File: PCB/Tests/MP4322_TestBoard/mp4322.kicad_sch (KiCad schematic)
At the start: 28 parts, among them J1 Conn_01x02, J2 Conn_01x02, U7 MP4322GDE-P

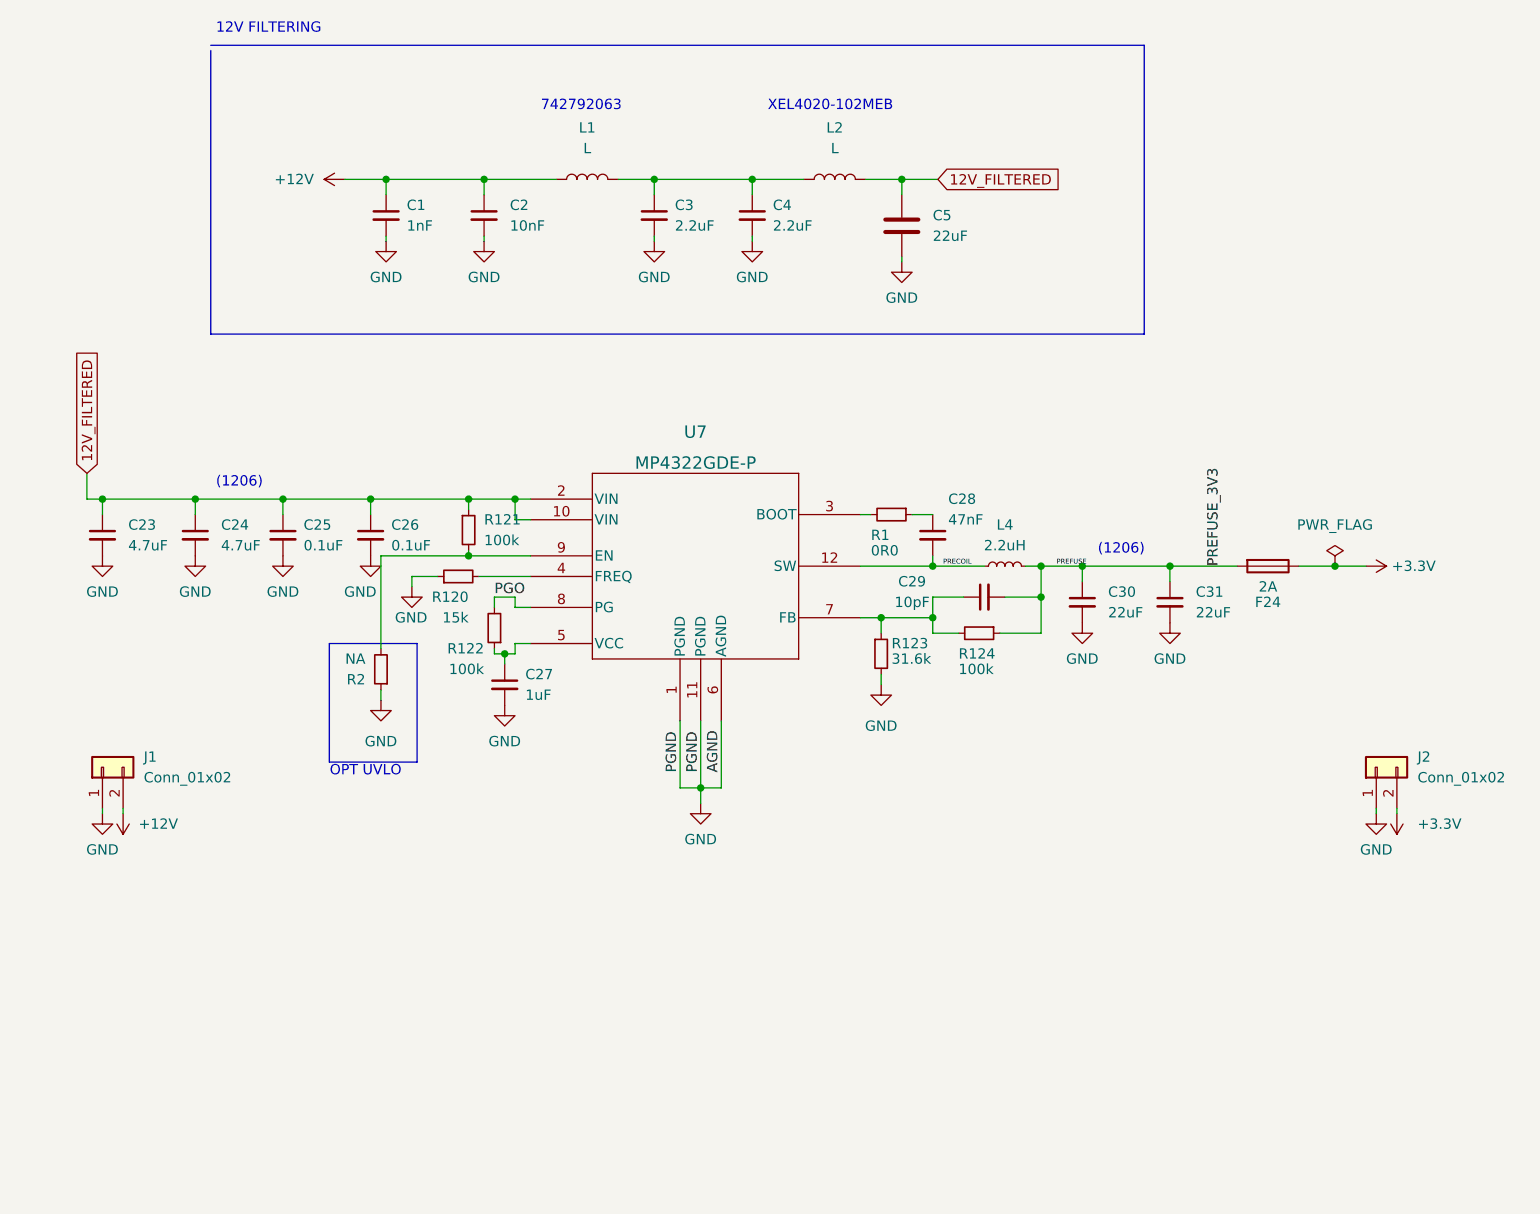
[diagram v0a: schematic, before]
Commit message: Generated production files for RP_MPQ5850 & MP4322 schematic change
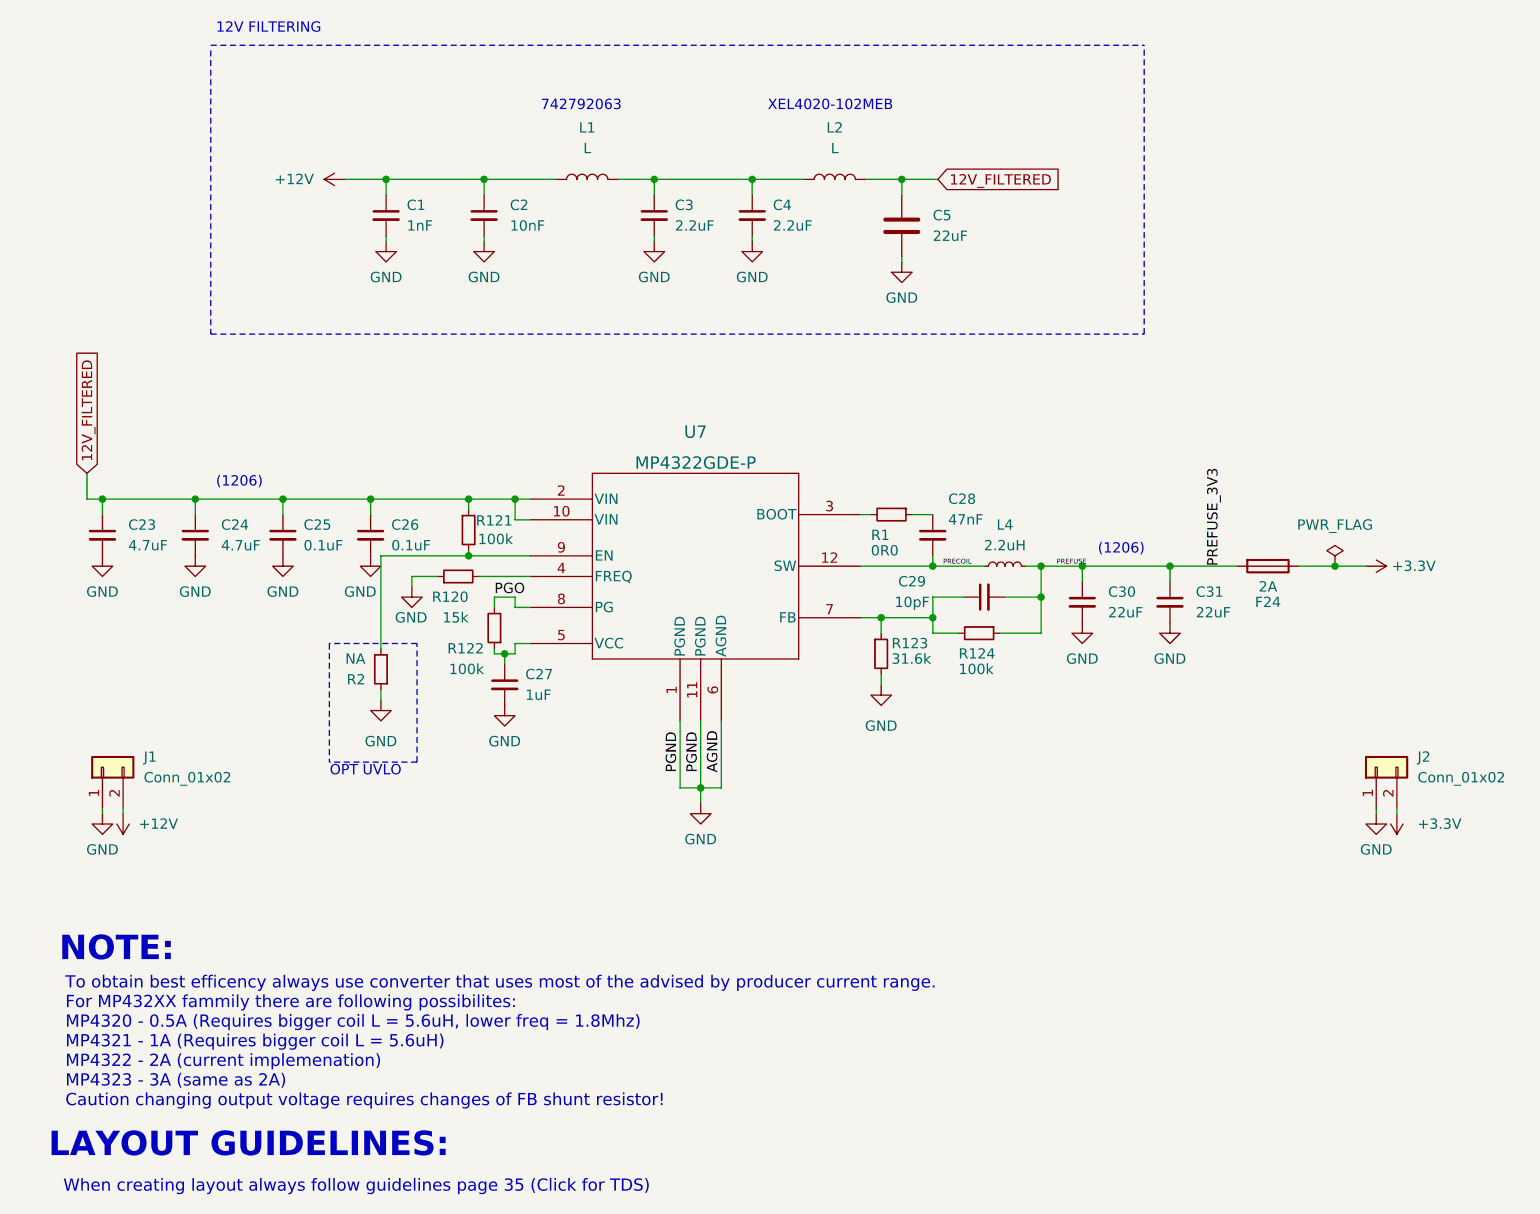
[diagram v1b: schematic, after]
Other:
- note added: "LAYOUT GUIDELINES:"
- note added: "NOTE:"
- note added: "To obtain best efficency always use converter that uses most of the advised by producer current range. For MP432XX fammily there are following possibilites: MP4320 - 0.5A (Requires bigger coil L = 5.6uH, lower freq = 1.8Mhz) MP4321 - 1A (Requires bigger coil L = 5.6uH) MP4322 - 2A (current implemenation) MP4323 - 3A (same as 2A) Caution changing output voltage requires changes of FB shunt resisto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"
- note added: "When creating layout always follow guidelines page 35 (Click for TDS)"
- company: (none) -> PGRacing Team
- title: (none) -> MP432X Power section

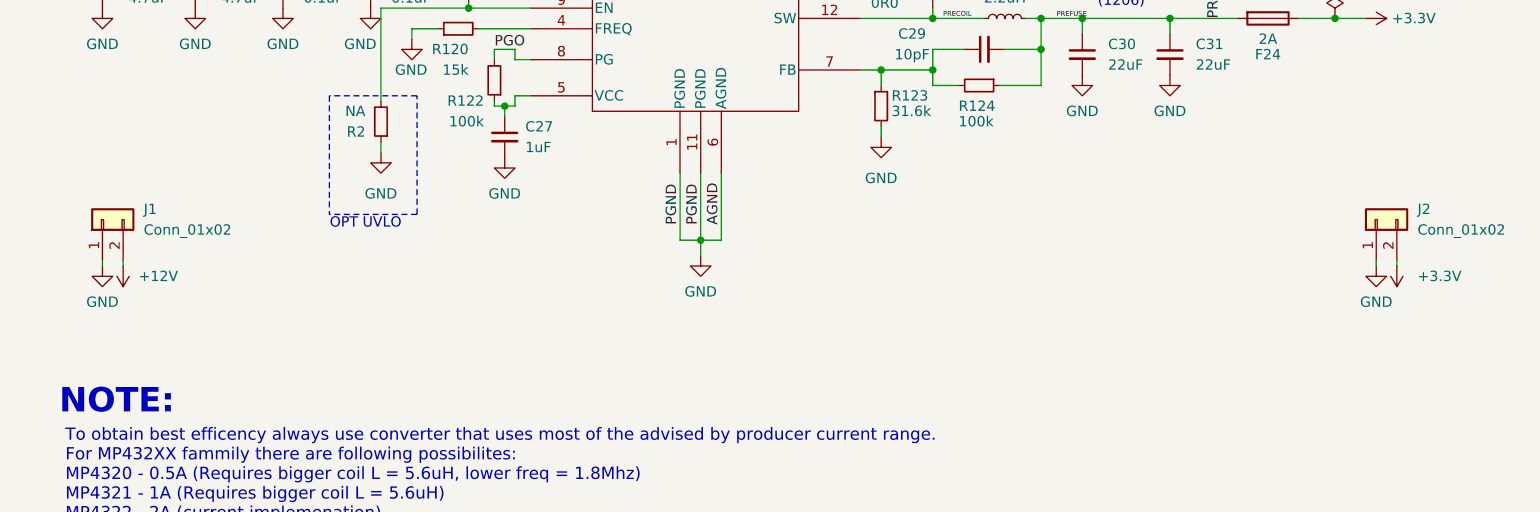
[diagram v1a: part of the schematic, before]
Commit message: Fixed memory and aux routing, fixed decoupling of MCU, fixed hse oscilator layout, fixed BTS500 input capacitors size and thermal, fixed via stiching on output channels, changed LP mos  traces to thiner ones, WIP mp4322 layout repliacte
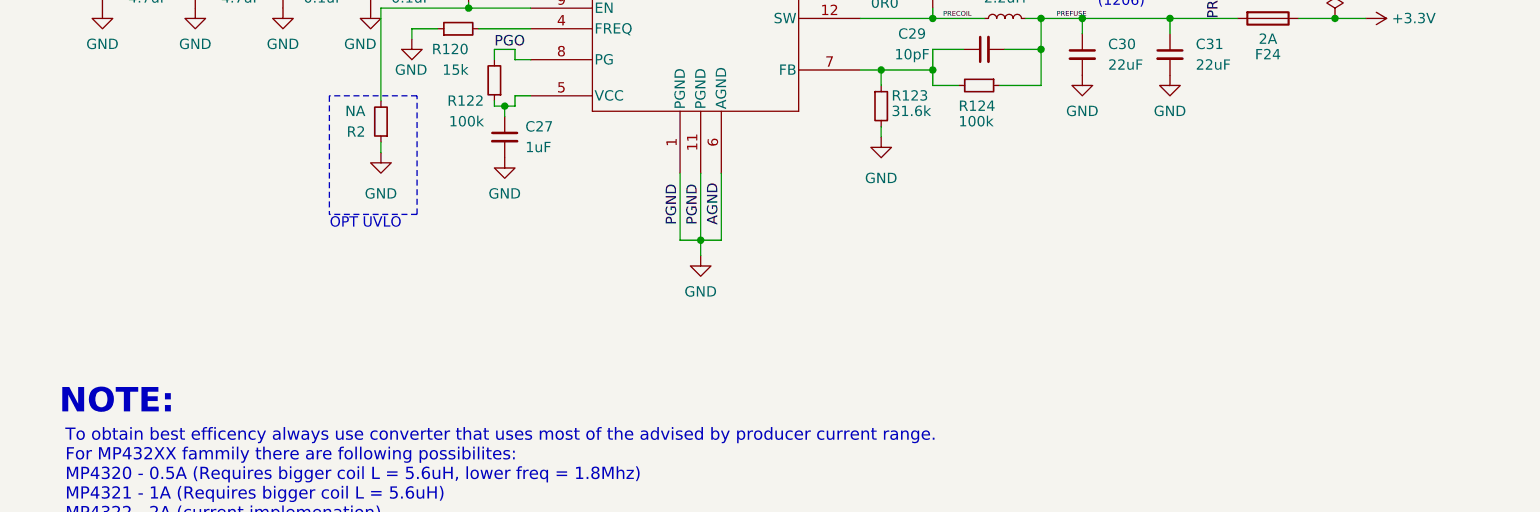
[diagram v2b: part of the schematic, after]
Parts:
- removed J1, J2: Conn_01x02, Connector_JST:JST_EH_B2B-EH-A_1x02_P2.50mm_Vertical, symbol Connector_Generic:Conn_01x02
